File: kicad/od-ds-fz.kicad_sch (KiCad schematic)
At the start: 26 parts

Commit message: finished sch, started footprint assignment
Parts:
- added C10: 2.2n, Capacitor_THT:C_Disc_D5.1mm_W3.2mm_P5.00mm, symbol Device:C_Polarized_US
- added C5: 220n, Capacitor_THT:CP_Radial_D7.5mm_P2.50mm, symbol Device:C_Polarized_US
- added C6: 100p, Capacitor_THT:C_Disc_D5.1mm_W3.2mm_P5.00mm, symbol Device:C
- added C7, C9: 1u, Capacitor_THT:CP_Radial_D7.5mm_P2.50mm, symbol Device:C_Polarized_US
- added C8: 470n, Capacitor_THT:CP_Radial_D7.5mm_P2.50mm, symbol Device:C_Polarized_US
- added D2, D3, D4, D5: D, Diode_THT:D_DO-15_P15.24mm_Horizontal, symbol Device:D
- added R10, R9: 1K, Resistor_THT:R_Axial_DIN0207_L6.3mm_D2.5mm_P10.16mm_Horizontal, symbol Device:R_US
- added R11, R12: 1M, Resistor_THT:R_Axial_DIN0207_L6.3mm_D2.5mm_P10.16mm_Horizontal, symbol Device:R_US
- added R13: 5K, Resistor_THT:R_Axial_DIN0207_L6.3mm_D2.5mm_P10.16mm_Horizontal, symbol Device:R_US
- added R14: 30K, Resistor_THT:R_Axial_DIN0207_L6.3mm_D2.5mm_P10.16mm_Horizontal, symbol Device:R_US
- added RVgain1, RVtone1: 220K, symbol Device:R_Potentiometer_US
- added RVvol1: 500, symbol Device:R_Potentiometer_US
- added SWclip1: SW_DPDT_x2, symbol Switch:SW_DPDT_x2
- C1, C2, C3, C4: renamed from C?; footprint (none) -> Capacitor_THT:CP_Radial_D7.5mm_P2.50mm
- R1, R2, R3, R4, R5, R6, R7, R8: renamed from R?; footprint (none) -> Resistor_THT:R_Axial_DIN0207_L6.3mm_D2.5mm_P10.16mm_Horizontal
- U1: renamed from U?; footprint (none) -> Package_DIP:DIP-14_W7.62mm
- gave numbers to parts that had none: 7
- renumbered JBat to JBat1, SWPow to SWPow1
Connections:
- net GND: now also C10.2, C5.2, D4.1 (K), D5.2 (A), R11.2, RVvol1.3
- net Vmid: now also R12.1
- net in: now also J1.T, R2.1, R3.1
- net at R8.2, U1.7: now also U1.10 (+)
- net at U1.12 (+): now also C8.1, R12.2
- net at U1.13 (-): now also U1.14, R14.1
- net at U1.1: now also U1.2 (-), C9.1
- net opamp4in: now reaches U1.3 (+)
- net opamp4in: now also C10.1, RVtone1.2, RVtone1.3
- net at SWPow1.4 (A): now also RVvol1.2
- net at U1.8: now also C6.2, C7.1, D2.1 (K), D3.2 (A), RVgain1.2, RVgain1.3
- net at U1.9 (-): now also C6.1, R9.1, RVgain1.1, SWclip1.2 (B)
- new net: R14.2, RVtone1.1
- new net: C9.2, R13.1
- new net: R13.2, RVvol1.1
- new net: D2.2 (A), D3.1 (K), SWclip1.1 (A)
- new net: C7.2, R10.1
- new net: D4.2 (A), D5.1 (K), SWclip1.6 (C)
- new net: C5.1, R9.2
- new net: C8.2, R10.2, R11.1, SWclip1.5 (B)
- no-connect marks 1 -> 3
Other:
- moved on the sheet: C2, C4, J1, J2, JBat1, R2, R3, R6, R7, R8, SWPow1A, SWPow1B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

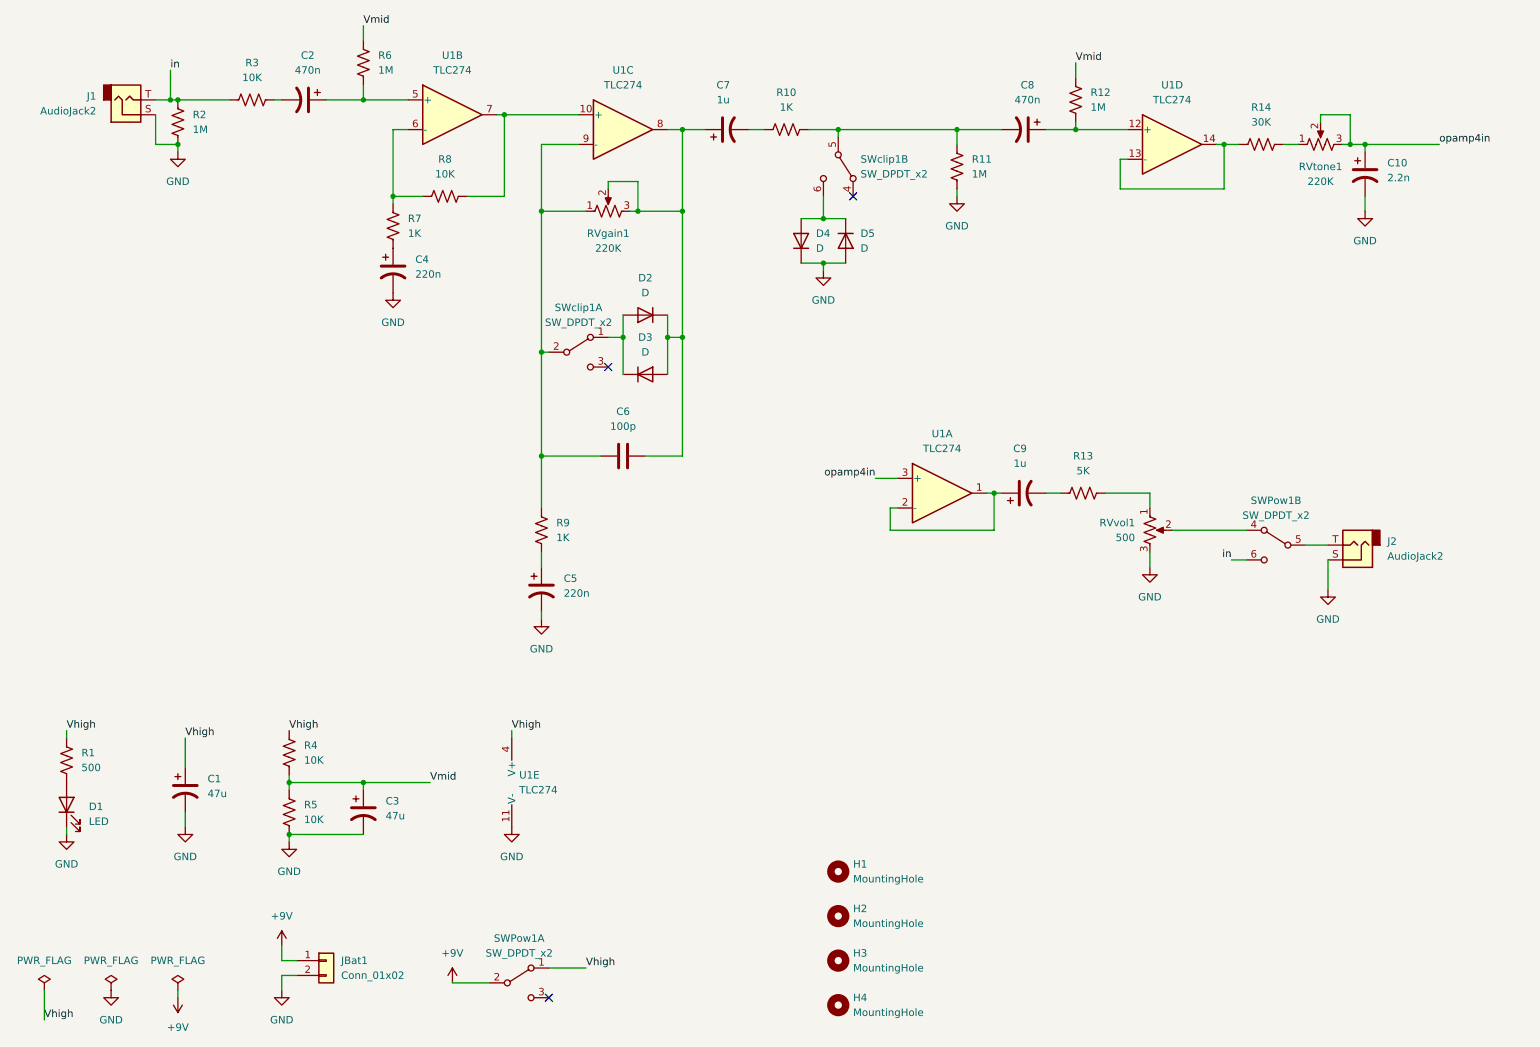
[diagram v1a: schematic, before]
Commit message: Placed components on PCB.
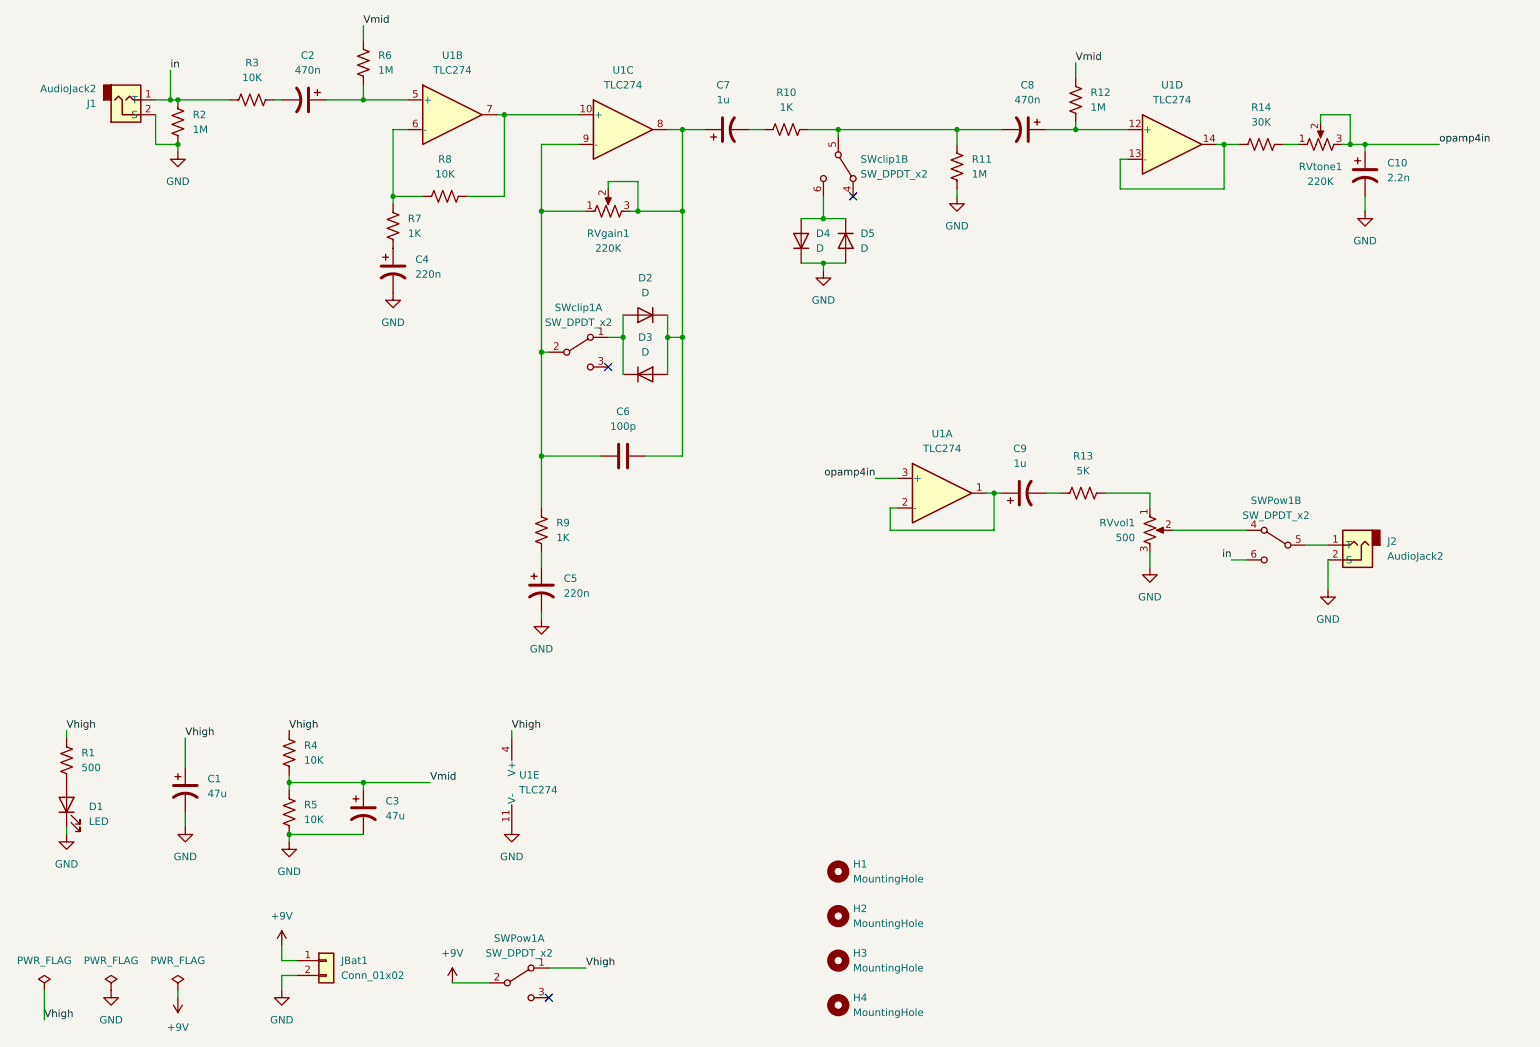
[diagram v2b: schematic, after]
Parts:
- D1, J1, J2, JBat1: footprint (none) -> Connector_Wire:SolderWire-0.5sqmm_1x02_P4.6mm_D0.9mm_OD2.1mm
- H1, H2, H3, H4: footprint (none) -> MountingHole:MountingHole_3.2mm_M3
- RVgain1, RVtone1, RVvol1: footprint (none) -> Connector_Wire:SolderWire-0.5sqmm_1x03_P4.6mm_D0.9mm_OD2.1mm
- SWPow1, SWclip1: footprint (none) -> Connector_Wire:SolderWire-0.5sqmm_1x06_P4.6mm_D0.9mm_OD2.1mm
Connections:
- net GND: now also J1.2 (S), J2.2 (S); no longer J1.S, J2.S
- net in: now also J1.1 (T); no longer J1.T
- net at SWPow1.5 (B): now also J2.1 (T); no longer J2.T

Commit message: routing and output files
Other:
- title: (none) -> OD-DS-FZ
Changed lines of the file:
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@@
 (kicad_sch (version 20211123) (generator eeschema)
   (paper "A4")
+  (title_block
+    (title "OD-DS-FZ")
+    (date "2022-10-18")
+    (rev "v0.0.0")
+  )
   (junction (at 129.54 76.2) (diameter 0) (color 0 0 0 0)
   )
